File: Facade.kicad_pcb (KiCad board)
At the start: 2 copper layers, 41.1 x 38.6 mm, 10 parts, among them J1 Conn_02x03_Odd_Even, J2 Conn_01x02, J4 Conn_01x02, J5 Conn_01x02

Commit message: v2 : ajout connetcteur plan de masse
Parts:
- added J3: Conn_01x01, Connector_PinSocket_2.54mm:PinSocket_1x01_P2.54mm_Vertical, F.Cu at (109.2, 55.9)
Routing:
- net GND: track 10.2 -> 25.7 mm
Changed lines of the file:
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@@
     (thickness 1.6)
     (drawings 3)
-    (tracks 30)
+    (tracks 33)
     (zones 0)
-    (modules 10)
+    (modules 11)
     (nets 11)
   )
@@
     )
   )
+  (module Connector_PinSocket_2.54mm:PinSocket_1x01_P2.54mm_Vertical (layer F.Cu)
+    (at 109.22 55.88)
+    (descr "Through hole straight socket strip, 1x01, 2.54mm pitch, single row (from Kicad 4.0.7), script generated")
+    (tags "Through hole socket strip THT 1x01 2.54mm single row")
+    (fp_text reference J3 (at 0 -2.77) (layer F.SilkS)
+      (effects (font (size 1 1) (thickness 0.15)))
+    )
+    (fp_text value Conn_01x01 (at 0 2.77) (layer F.Fab)
+      (effects (font (size 1 1) (thickness 0.15)))
+    )
+    (fp_line (start -1.27 -1.27) (end 0.635 -1.27) (layer F.Fab) (width 0.1))
+    (fp_line (start 0.635 -1.27) (end 1.27 -0.635) (layer F.Fab) (width 0.1))
+    (fp_line (start 1.27 -0.635) (end 1.27 1.27) (layer F.Fab) (width 0.1))
+    (fp_line (start 1.27 1.27) (end -1.27 1.27) (layer F.Fab) (width 0.1))
+    (fp_line (start -1.27 1.27) (end -1.27 -1.27) (layer F.Fab) (width 0.1))
+    (fp_line (start -1.33 1.33) (end 1.33 1.33) (layer F.SilkS) (width 0.12))
+    (fp_line (start -1.33 1.21) (end -1.33 1.33) (layer F.SilkS) (width 0.12))
+    (fp_line (start 1.33 1.21) (end 1.33 1.33) (layer F.SilkS) (width 0.12))
+    (fp_line (start 1.33 -1.33) (end 1.33 0) (layer F.SilkS) (width 0.12))
+    (fp_line (start 0 -1.33) (end 1.33 -1.33) (layer F.SilkS) (width 0.12))
+    (fp_line (start -1.8 -1.8) (end 1.75 -1.8) (layer F.CrtYd) (width 0.05))
+    (fp_line (start 1.75 -1.8) (end 1.75 1.75) (layer F.CrtYd) (width 0.05))
+    (fp_line (start 1.75 1.75) (end -1.8 1.75) (layer F.CrtYd) (width 0.05))
+    (fp_line (start -1.8 1.75) (end -1.8 -1.8) (layer F.CrtYd) (width 0.05))
+    (fp_text user %R (at 0 0) (layer F.Fab)
+      (effects (font (size 1 1) (thickness 0.15)))
+    )
+    (pad 1 thru_hole rect (at 0 0) (size 1.7 1.7) (drill 1) (layers *.Cu *.Mask)
+      (net 1 GND))
+    (model ${KISYS3DMOD}/Connector_PinSocket_2.54mm.3dshapes/PinSocket_1x01_P2.54mm_Vertical.wrl
+      (at (xyz 0 0 0))
+      (scale (xyz 1 1 1))
+      (rotate (xyz 0 0 0))
+    )
+  )
   (gr_circle (center 72.39 77.47) (end 73.89 77.47) (layer Edge.Cuts) (width 0.15))
   (gr_circle (center 110.49 41.91) (end 111.99 41.91) (layer Edge.Cuts) (width 0.2))
@@
   )
   (segment (start 81.28 44.45) (end 91.44 44.45) (width 0.762) (layer F.Cu) (net 1))
+  (segment (start 103.262 44.45) (end 101.6 44.45) (width 0.762) (layer B.Cu) (net 1))
+  (segment (start 109.22 50.408) (end 103.262 44.45) (width 0.762) (layer B.Cu) (net 1))
+  (segment (start 109.22 55.88) (end 109.22 50.408) (width 0.762) (layer B.Cu) (net 1))
   (segment (start 81.28 54.61) (end 81.28 46.99) (width 0.762) (layer B.Cu) (net 2))
   (segment (start 91.44 53.34) (end 91.44 46.99) (width 0.762) (layer B.Cu) (net 3))

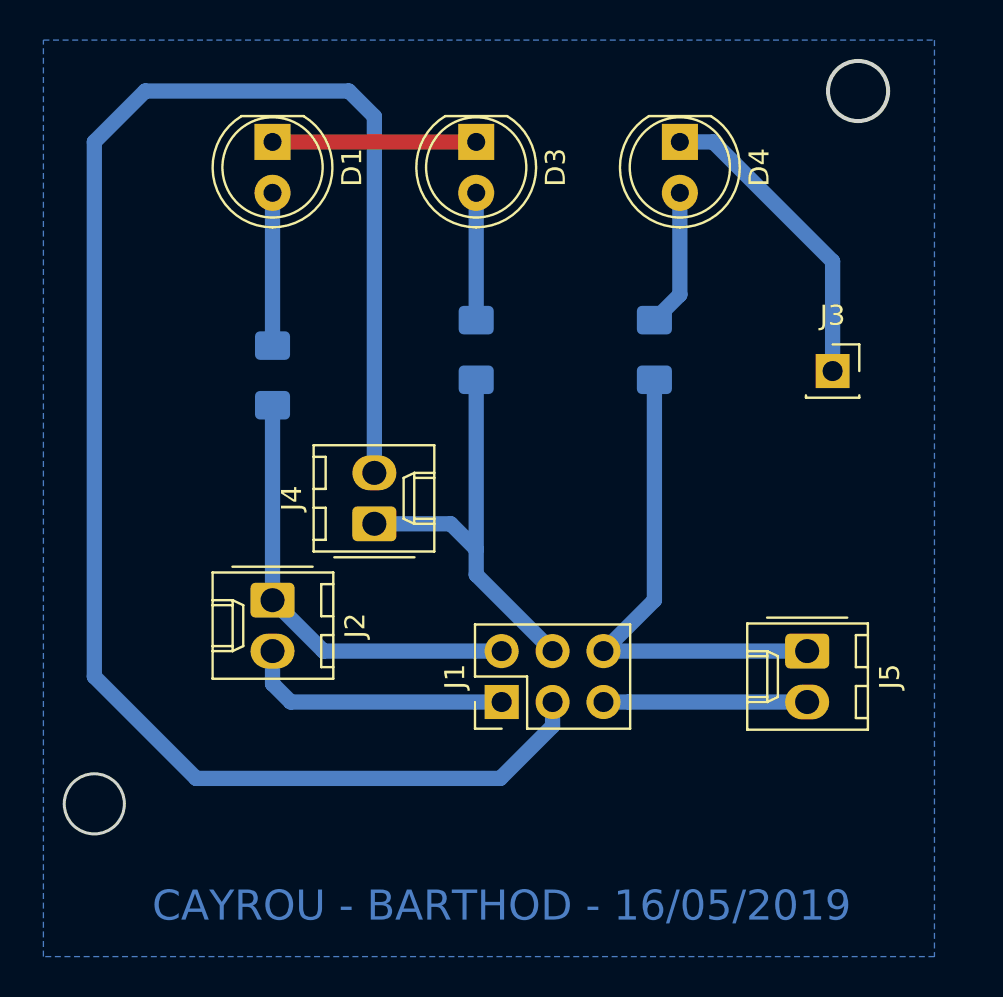
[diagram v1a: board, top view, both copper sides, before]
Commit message: Use new connector
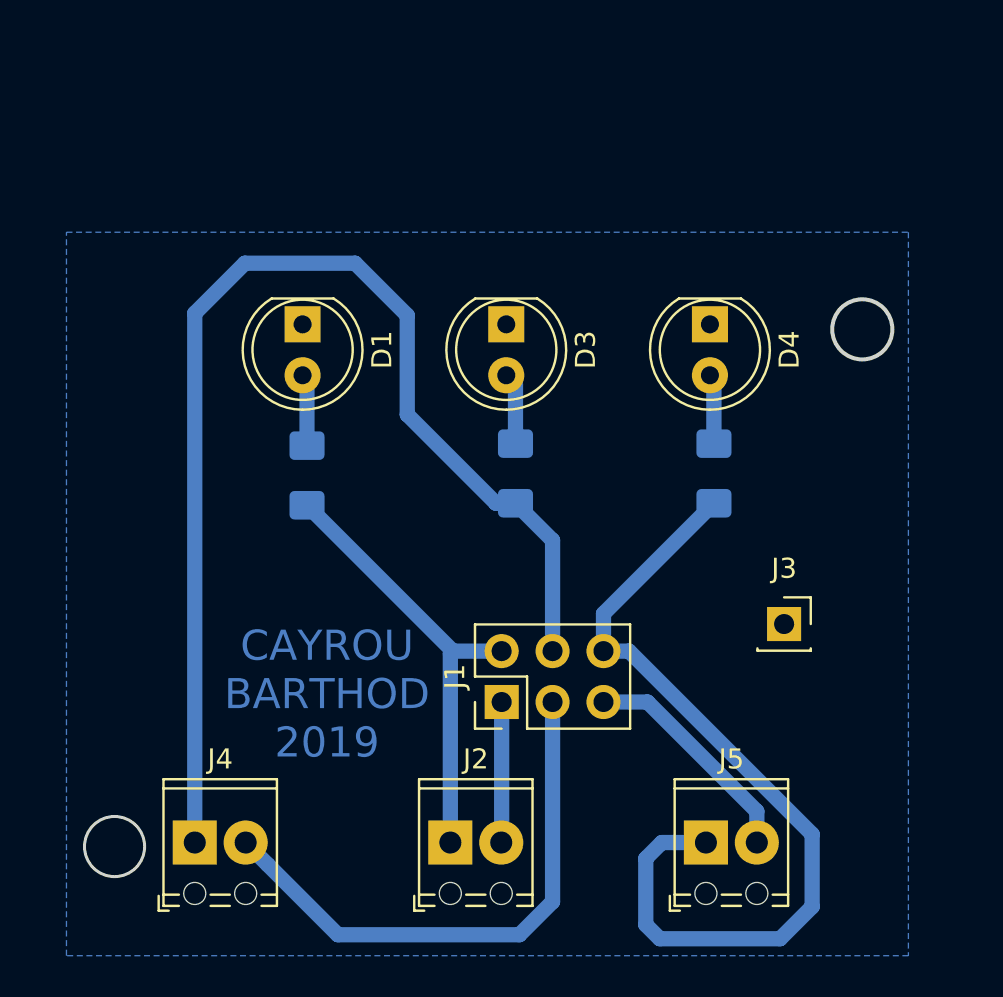
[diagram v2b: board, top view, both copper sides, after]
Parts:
- J2, J4, J5: footprint Connector_Molex:Molex_KK-254_AE-6410-02A_1x02_P2.54mm_Vertical -> TerminalBlock_Phoenix:TerminalBlock_Phoenix_MPT-0,5-2-2.54_1x02_P2.54mm_Horizontal
- moved J4 18.3 mm to (77.4, 79.4), turned to 0 degrees
- moved J2 15.0 mm to (90.2, 79.4), turned to 0 degrees
- moved J3 12.8 mm to (106.8, 68.5)
- moved J5 10.8 mm to (102.9, 79.4), turned to 0 degrees
- moved D1 9.22 mm to (82.8, 53.5)
- moved D3 9.22 mm to (92.9, 53.5)
- moved D4 9.22 mm to (103.1, 53.5)
- moved R4 6.84 mm to (103.3, 61.0)
- moved R3 6.46 mm to (93.4, 61.0)
- moved R1 5.28 mm to (83.0, 61.1)
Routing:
- net +7.5V: track 87.2 -> 27.9 mm
- net Net-(J1-Pad4): track 20.7 -> 59.4 mm
- net GND: track 25.7 -> 0.00 mm
- net Net-(J1-Pad6): track 24.7 -> 43.3 mm
- net +5V: track 13.4 -> 7.02 mm
- net Net-(D1-Pad2): track 7.62 -> 3.60 mm
- net Net-(D4-Pad2): track 6.88 -> 3.49 mm
- net Net-(D3-Pad2): track 6.35 -> 3.60 mm
- net +15V: track 10.2 -> 11.5 mm
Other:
- board size 41.1 x 38.6 mm -> 40.3 x 28.8 mm
- board text added: "CAYROU BARTHOD 2019"
- board text removed: "CAYROU - BARTHOD - 16/05/2019"
